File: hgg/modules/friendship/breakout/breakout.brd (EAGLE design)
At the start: 91 x 29.5 mm, 7 parts, among them IC1 MAX481CSA, IC2 MAX481CSA

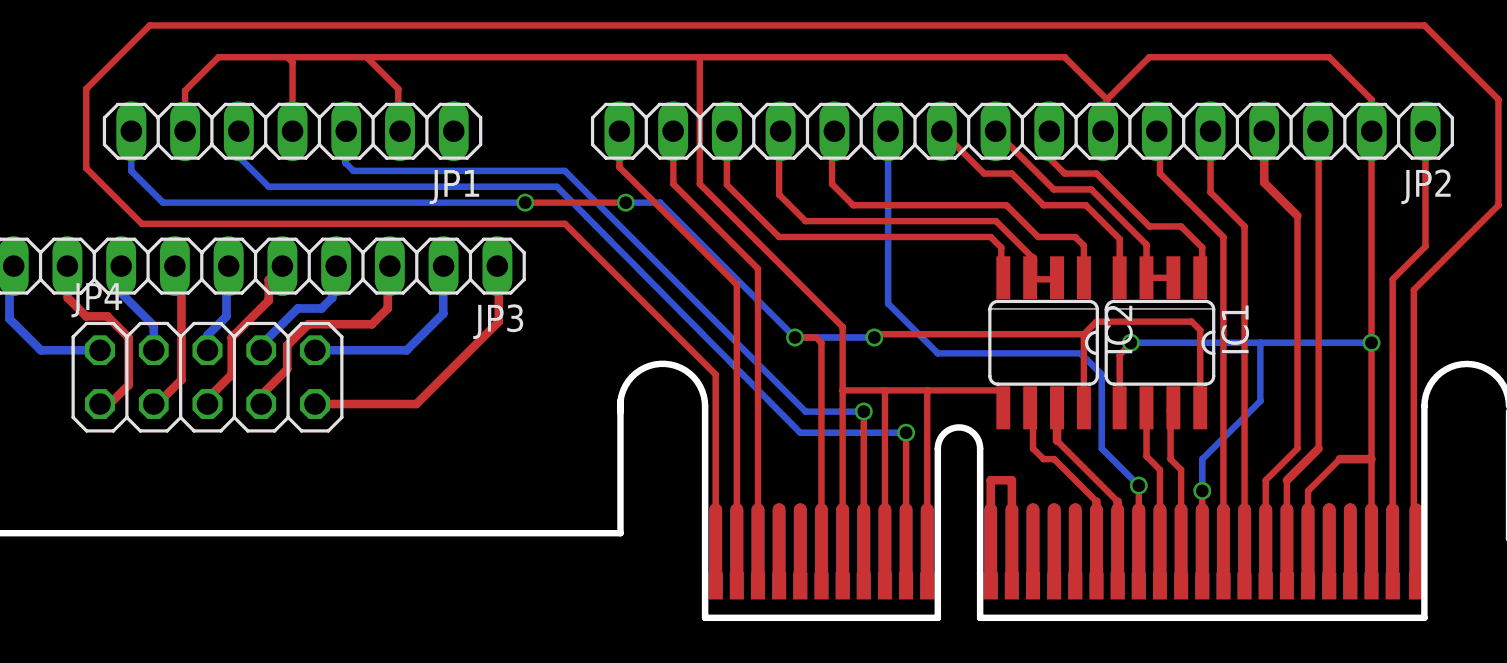
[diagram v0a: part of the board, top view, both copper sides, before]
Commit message: max485 now running @ 5V vcc
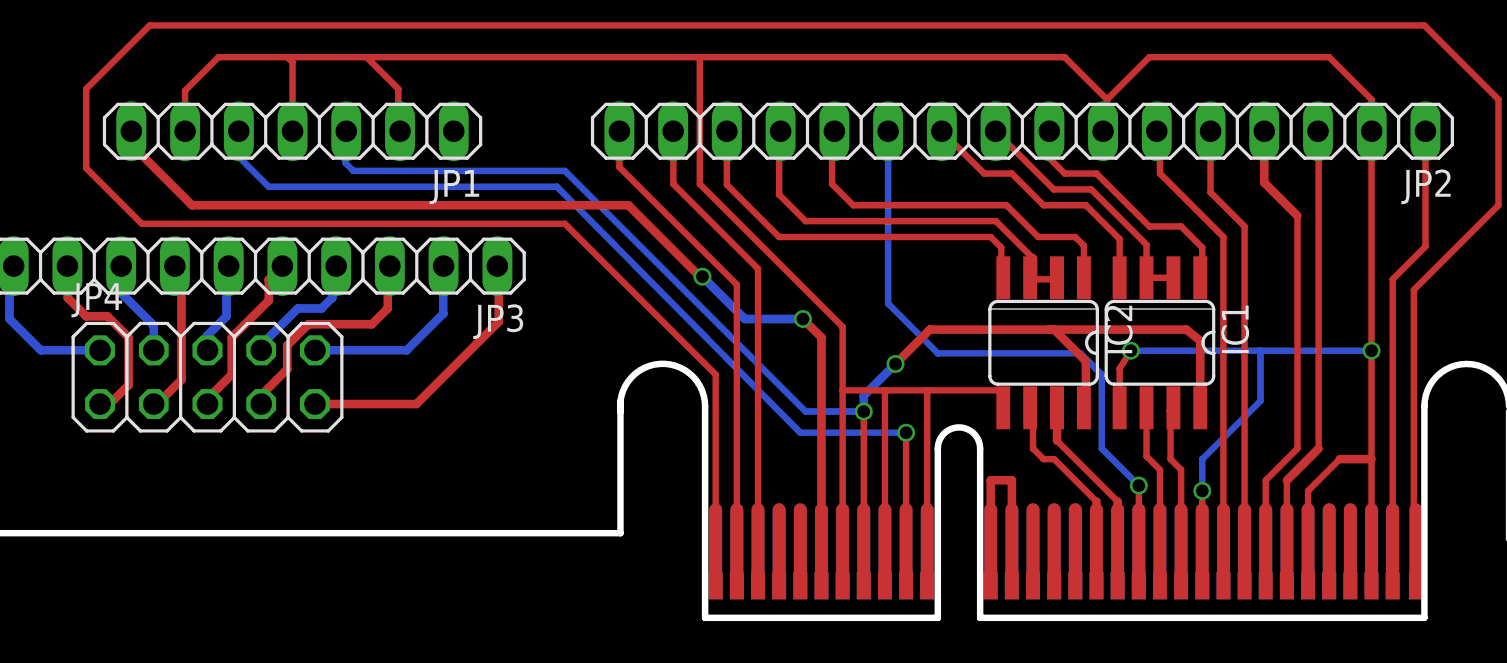
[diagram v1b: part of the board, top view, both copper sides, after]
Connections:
- removed net N$18: JP1.3, U$1.A08(+5V)
- new net 3V3: JP1.7, U$1.A06(+3V3)
- net VCC: now also JP1.3, U$1.A08(+5V); no longer JP1.7, U$1.A06(+3V3)
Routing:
- net 3V3: track 0.00 -> 48.8 mm, vias 0 -> 2
- net N$18: track 39.1 -> 0.00 mm, vias 1 -> 0
- net VCC: track 76.1 -> 64.8 mm, vias 4 -> 2
- net GND: track 183.7 -> 182.9 mm
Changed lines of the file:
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@@
 <wire x1="76.5" y1="24.5" x2="76.5" y2="23.01" width="0.3048" layer="1"/>
 <wire x1="76.5" y1="23.01" x2="76.51" y2="23" width="0.4064" layer="1"/>
-<via x="76.5" y="13" extent="1-16" drill="0.6"/>
-<wire x1="65.125" y1="13" x2="71.25" y2="13" width="0.3048" layer="16"/>
-<wire x1="71.25" y1="13" x2="76.5" y2="13" width="0.3048" layer="16"/>
-<wire x1="76.5" y1="13" x2="76.5" y2="22.99" width="0.3048" layer="1"/>
+<via x="76.5" y="12.625" extent="1-16" drill="0.6"/>
+<wire x1="65.125" y1="12.625" x2="71.25" y2="12.625" width="0.3048" layer="16"/>
+<wire x1="71.25" y1="12.625" x2="76.5" y2="12.625" width="0.3048" layer="16"/>
+<wire x1="76.5" y1="12.625" x2="76.5" y2="22.99" width="0.3048" layer="1"/>
 <wire x1="76.5" y1="22.99" x2="76.51" y2="23" width="0.4064" layer="1"/>
 <wire x1="76.5" y1="1.51" x2="76.5" y2="7.5" width="0.3048" layer="1"/>
-<wire x1="76.5" y1="7.5" x2="76.5" y2="13" width="0.3048" layer="1"/>
+<wire x1="76.5" y1="7.5" x2="76.5" y2="12.625" width="0.3048" layer="1"/>
 <wire x1="73.5" y1="1.51" x2="73.5" y2="6" width="0.3048" layer="1"/>
 <wire x1="73.5" y1="6" x2="75" y2="7.5" width="0.3048" layer="1"/>
@@
 <wire x1="68.5" y1="6" x2="68.5" y2="7.5" width="0.3048" layer="16"/>
 <wire x1="68.5" y1="7.5" x2="71.25" y2="10.25" width="0.3048" layer="16"/>
-<wire x1="71.25" y1="10.25" x2="71.25" y2="13" width="0.3048" layer="16"/>
-<wire x1="64.595" y1="9.9266" x2="64.595" y2="12.405" width="0.3048" layer="1"/>
-<wire x1="64.595" y1="12.405" x2="65.125" y2="13" width="0.3048" layer="1"/>
-<via x="65.125" y="13" extent="1-16" drill="0.6"/>
+<wire x1="71.25" y1="10.25" x2="71.25" y2="12.625" width="0.3048" layer="16"/>
+<wire x1="64.595" y1="9.9266" x2="64.595" y2="11.78" width="0.3048" layer="1"/>
+<wire x1="64.595" y1="11.78" x2="65.125" y2="12.625" width="0.3048" layer="1"/>
+<via x="65.125" y="12.625" extent="1-16" drill="0.6"/>
 <wire x1="51.5" y1="1.51" x2="51.5" y2="10.75" width="0.3048" layer="1"/>
 <contactref element="U$1" pad="A09(GND)"/>
@@
 <contactref element="IC1" pad="8"/>
 <contactref element="IC2" pad="8"/>
-<wire x1="62.905" y1="9.9266" x2="62.905" y2="13.405" width="0.3048" layer="1"/>
-<wire x1="62.905" y1="13.405" x2="63.5" y2="14" width="0.3048" layer="1"/>
-<wire x1="68.405" y1="9.9266" x2="68.405" y2="13.595" width="0.3048" layer="1"/>
-<wire x1="68.405" y1="13.595" x2="68" y2="14" width="0.3048" layer="1"/>
-<wire x1="63.5" y1="14" x2="68" y2="14" width="0.3048" layer="1"/>
-<contactref element="U$1" pad="A06(+3V3)"/>
-<wire x1="50.5" y1="1.51" x2="50.5" y2="13" width="0.3048" layer="1"/>
-<contactref element="JP1" pad="7"/>
-<wire x1="17.88" y1="23" x2="17.88" y2="21.12" width="0.3048" layer="16"/>
-<wire x1="17.88" y1="21.12" x2="19.375" y2="19.625" width="0.3048" layer="16"/>
-<wire x1="19.375" y1="19.625" x2="36.5" y2="19.625" width="0.3048" layer="16"/>
-<via x="36.5" y="19.625" extent="1-16" drill="0.6"/>
-<wire x1="36.5" y1="19.625" x2="41.25" y2="19.625" width="0.3048" layer="1"/>
-<via x="41.25" y="19.625" extent="1-16" drill="0.6"/>
-<wire x1="41.25" y1="19.625" x2="42.875" y2="19.625" width="0.3048" layer="16"/>
-<wire x1="42.875" y1="19.625" x2="49.25" y2="13.25" width="0.3048" layer="16"/>
-<via x="49.25" y="13.25" extent="1-16" drill="0.6"/>
-<wire x1="49.25" y1="13.25" x2="50.25" y2="13.25" width="0.3048" layer="1"/>
-<wire x1="50.25" y1="13.25" x2="50.5" y2="13" width="0.3048" layer="1"/>
-<wire x1="62.905" y1="13.405" x2="53.155" y2="13.405" width="0.3048" layer="1"/>
-<wire x1="53.155" y1="13.405" x2="53" y2="13.25" width="0.3048" layer="1"/>
-<via x="53" y="13.25" extent="1-16" drill="0.6"/>
-<wire x1="53" y1="13.25" x2="49.25" y2="13.25" width="0.3048" layer="16"/>
+<contactref element="U$1" pad="A08(+5V)"/>
+<contactref element="JP1" pad="3"/>
+<wire x1="52.5" y1="1.51" x2="52.5" y2="9.75" width="0.3048" layer="1"/>
+<via x="52.5" y="9.75" extent="1-16" drill="0.6"/>
+<wire x1="52.5" y1="9.75" x2="49.75" y2="9.75" width="0.3048" layer="16"/>
+<wire x1="49.75" y1="9.75" x2="38.375" y2="21.125" width="0.3048" layer="16"/>
+<wire x1="38.375" y1="21.125" x2="28.375" y2="21.125" width="0.3048" layer="16"/>
+<wire x1="28.375" y1="21.125" x2="28" y2="21.5" width="0.3048" layer="16"/>
+<wire x1="28" y1="21.5" x2="28" y2="22.71" width="0.3048" layer="16"/>
+<wire x1="28" y1="22.71" x2="28.04" y2="23" width="0.3048" layer="16"/>
+<wire x1="52.5" y1="9.75" x2="52.5" y2="10.5" width="0.4064" layer="16"/>
+<wire x1="52.5" y1="10.5" x2="54" y2="12" width="0.4064" layer="16"/>
+<via x="54" y="12" extent="1-16" drill="0.6"/>
+<wire x1="54" y1="12" x2="55.625" y2="13.625" width="0.4064" layer="1"/>
+<wire x1="55.625" y1="13.625" x2="61.25" y2="13.625" width="0.4064" layer="1"/>
+<wire x1="61.375" y1="13.625" x2="61.5" y2="13.625" width="0.4064" layer="1"/>
+<wire x1="61.5" y1="13.625" x2="63" y2="12.125" width="0.4064" layer="1"/>
+<wire x1="63" y1="12.125" x2="63" y2="10.0216" width="0.4064" layer="1"/>
+<wire x1="63" y1="10.0216" x2="62.905" y2="9.9266" width="0.4064" layer="1"/>
+<wire x1="68.405" y1="9.9266" x2="68.405" y2="13.095" width="0.4064" layer="1"/>
+<wire x1="68.405" y1="13.095" x2="67.75" y2="13.625" width="0.4064" layer="1"/>
+<wire x1="67.75" y1="13.625" x2="61.5" y2="13.625" width="0.4064" layer="1"/>
+<wire x1="61.375" y1="13.625" x2="61.25" y2="13.625" width="0.4064" layer="1"/>
 </signal>
 <signal name="N$15">
@@
 <wire x1="54.5" y1="8.75" x2="54.5" y2="1.51" width="0.3048" layer="1"/>
 </signal>
-<signal name="N$18">
-<contactref element="U$1" pad="A08(+5V)"/>
-<contactref element="JP1" pad="3"/>
-<wire x1="52.5" y1="1.51" x2="52.5" y2="9.75" width="0.3048" layer="1"/>
-<via x="52.5" y="9.75" extent="1-16" drill="0.6"/>
-<wire x1="52.5" y1="9.75" x2="49.75" y2="9.75" width="0.3048" layer="16"/>
-<wire x1="49.75" y1="9.75" x2="38.375" y2="21.125" width="0.3048" layer="16"/>
-<wire x1="38.375" y1="21.125" x2="28.375" y2="21.125" width="0.3048" layer="16"/>
-<wire x1="28.375" y1="21.125" x2="28" y2="21.5" width="0.3048" layer="16"/>
-<wire x1="28" y1="21.5" x2="28" y2="22.71" width="0.3048" layer="16"/>
-<wire x1="28" y1="22.71" x2="28.04" y2="23" width="0.3048" layer="16"/>
-</signal>
 <signal name="N$22">
 <contactref element="JP4" pad="2"/>
@@
 <wire x1="35.25" y1="16.555" x2="35.18" y2="16.625" width="0.4064" layer="1"/>
 </signal>
+<signal name="3V3">
+<contactref element="U$1" pad="A06(+3V3)"/>
+<contactref element="JP1" pad="7"/>
+<wire x1="50.5" y1="1.51" x2="50.5" y2="13.25" width="0.4064" layer="1"/>
+<wire x1="50.5" y1="13.25" x2="49.625" y2="14.125" width="0.4064" layer="1"/>
+<via x="49.625" y="14.125" extent="1-16" drill="0.6"/>
+<wire x1="49.625" y1="14.125" x2="46.875" y2="14.125" width="0.4064" layer="16"/>
+<wire x1="46.875" y1="14.125" x2="44.875" y2="16.125" width="0.4064" layer="16"/>
+<via x="44.875" y="16.125" extent="1-16" drill="0.6"/>
+<wire x1="44.875" y1="16.125" x2="44.75" y2="16.125" width="0.4064" layer="1"/>
+<wire x1="44.75" y1="16.125" x2="41.375" y2="19.5" width="0.4064" layer="1"/>
+<wire x1="41.375" y1="19.5" x2="20.75" y2="19.5" width="0.4064" layer="1"/>
+<wire x1="20.75" y1="19.5" x2="17.875" y2="22.375" width="0.4064" layer="1"/>
+<wire x1="17.875" y1="22.375" x2="17.875" y2="22.995" width="0.4064" layer="1"/>
+<wire x1="17.875" y1="22.995" x2="17.88" y2="23" width="0.4064" layer="1"/>
+</signal>
 </signals>

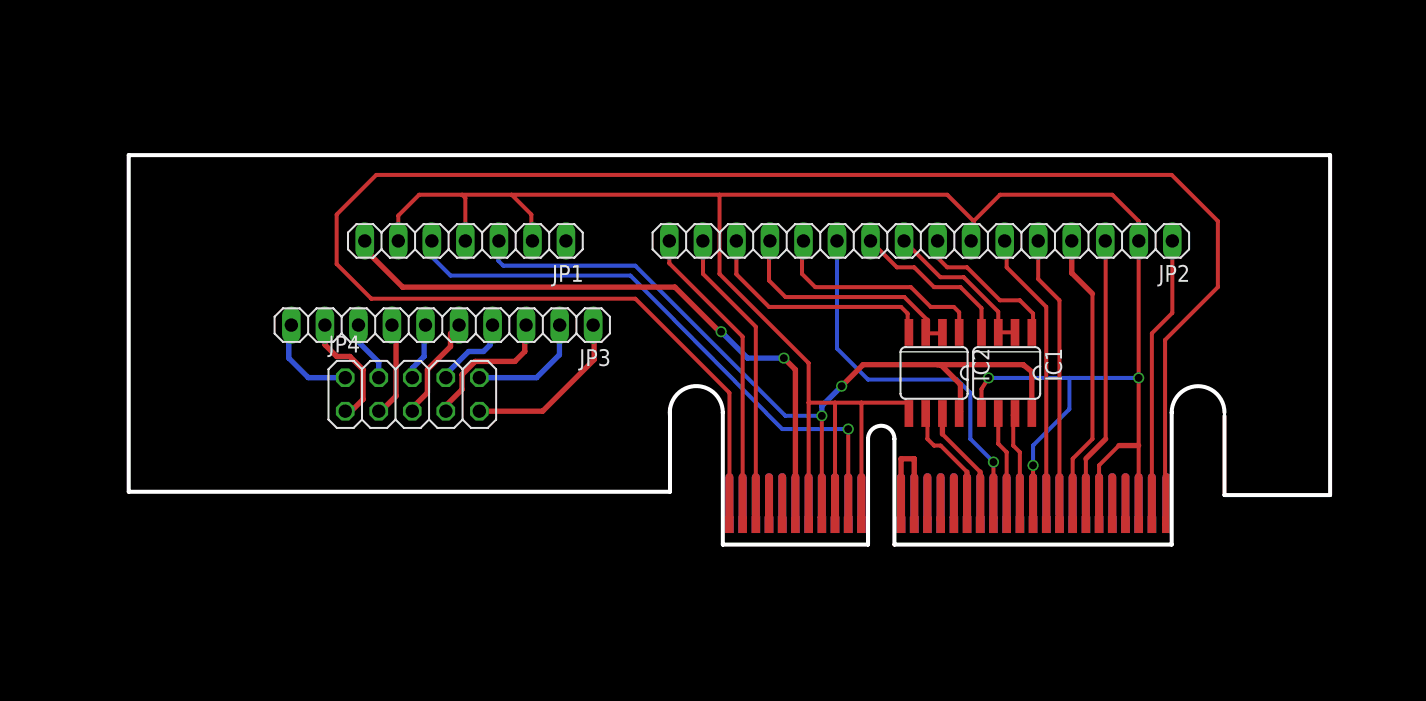
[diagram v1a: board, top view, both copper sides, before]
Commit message: swapped sides of the pcb
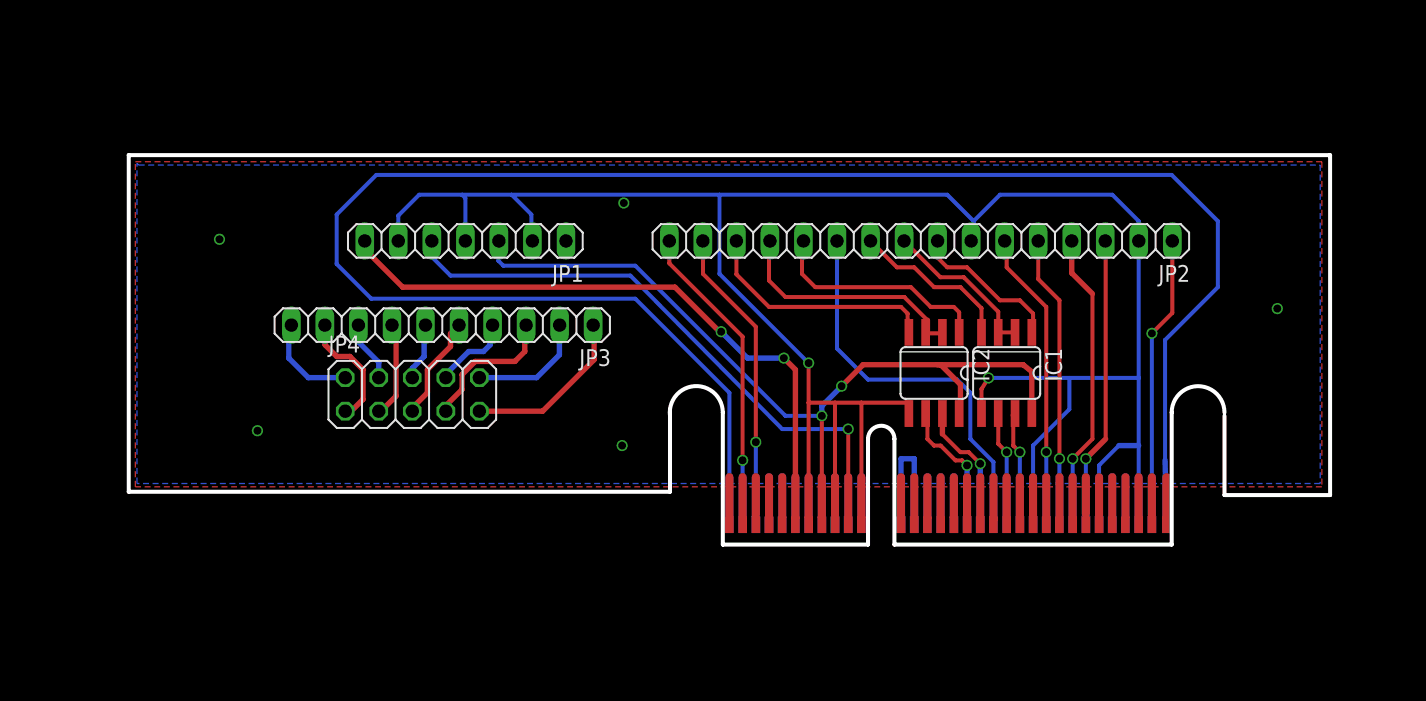
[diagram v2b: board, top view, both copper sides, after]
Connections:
- removed net N$13: JP1.5, U$1.A10(+12V)
- new net 12V: JP1.5, U$1.B10(+12V)
- net 3V3: now also U$1.B06(+3V3); no longer U$1.A06(+3V3)
- net GND: now also U$1.B07(GND), U$1.B09(GND), U$1.B11(GND); no longer U$1.A07(GND), U$1.A09(GND), U$1.A11(GND)
- net VCC: no longer U$1.A08(+5V)
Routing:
- net N$13: track 45.4 -> 0.00 mm, vias 1 -> 0
- net 12V: track 0.00 -> 45.4 mm, vias 0 -> 1
- net GND: track 182.9 -> 182.4 mm, vias 3 -> 9
- net N$3: track 9.60 -> 9.97 mm, vias 0 -> 1
- net N$2: track 10.0 -> 10.3 mm, vias 0 -> 1
- net N$19: vias 0 -> 1
- net N$9: vias 0 -> 1
- net N$7: vias 0 -> 1
- net N$6: vias 0 -> 1
- net N$5: vias 0 -> 1
- net N$23: vias 0 -> 1
- net N$21: vias 0 -> 1
- net N$20: vias 0 -> 1
- net N$17: vias 0 -> 1
- net N$10: vias 1 -> 0
- added copper zone on layer 1, net GND
- added copper zone on layer 16, net GND

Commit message: few improvements
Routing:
- net N$23: vias 1 -> 0
- net N$20: vias 1 -> 2
- net N$19: vias 1 -> 2
- net N$17: vias 1 -> 2
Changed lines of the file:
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@@
 <contactref element="IC2" pad="6"/>
 <wire x1="63.5" y1="1.51" x2="63.5" y2="6" width="0.4064" layer="16"/>
-<wire x1="63.5" y1="6" x2="63.125" y2="6.375" width="0.3048" layer="1"/>
-<wire x1="63.125" y1="6.375" x2="62.625" y2="6.375" width="0.3048" layer="1"/>
-<wire x1="62.625" y1="6.375" x2="61.5" y2="7.5" width="0.3048" layer="1"/>
-<wire x1="61.5" y1="7.5" x2="61" y2="7.5" width="0.3048" layer="1"/>
-<wire x1="61" y1="7.5" x2="60.5" y2="8" width="0.3048" layer="1"/>
+<wire x1="63.5" y1="6" x2="63.125" y2="6.375" width="0.3048" layer="16"/>
+<wire x1="63.125" y1="6.375" x2="62.25" y2="6.375" width="0.3048" layer="16"/>
+<wire x1="62.25" y1="6.375" x2="61.125" y2="7.5" width="0.3048" layer="16"/>
+<wire x1="61.125" y1="7.5" x2="60.5" y2="8" width="0.3048" layer="1"/>
 <wire x1="60.5" y1="8" x2="60.5" y2="10" width="0.3048" layer="1"/>
-<via x="63.5" y="6" extent="1-16" drill="0.6"/>
 <wire x1="60.5" y1="10" x2="60.365" y2="9.9266" width="0" layer="19" extent="1-1"/>
+<via x="61.125" y="7.5" extent="1-16" drill="0.6"/>
 </signal>
 <signal name="N$3">
@@
 <wire x1="69.5" y1="1.51" x2="69.5" y2="7.01" width="0.3048" layer="16"/>
 <wire x1="69.5" y1="7.01" x2="69.5" y2="18" width="0.3048" layer="1"/>
-<wire x1="69.5" y1="18" x2="66.5" y2="21" width="0.3048" layer="1"/>
-<wire x1="66.5" y1="21" x2="66.5" y2="22.85" width="0.3048" layer="1"/>
-<wire x1="66.5" y1="22.85" x2="66.35" y2="23" width="0.4064" layer="1"/>
+<wire x1="69.5" y1="18" x2="66.5" y2="21" width="0.3048" layer="16"/>
+<wire x1="66.5" y1="21" x2="66.5" y2="22.85" width="0.3048" layer="16"/>
+<wire x1="66.5" y1="22.85" x2="66.35" y2="23" width="0.4064" layer="16"/>
 <via x="69.5" y="7.01" extent="1-16" drill="0.6"/>
+<via x="69.5" y="18" extent="1-16" drill="0.6"/>
 </signal>
 <signal name="N$19">
 <contactref element="U$1" pad="A24(SLOWCLKCLK)"/>
 <contactref element="JP2" pad="5"/>
-<wire x1="68.89" y1="23" x2="68.89" y2="20.11" width="0.3048" layer="1"/>
-<wire x1="68.89" y1="20.11" x2="70.5" y2="18.5" width="0.3048" layer="1"/>
+<wire x1="68.89" y1="23" x2="68.89" y2="20.11" width="0.3048" layer="16"/>
+<wire x1="68.89" y1="20.11" x2="70.5" y2="18.5" width="0.3048" layer="16"/>
 <wire x1="70.5" y1="18.5" x2="70.5" y2="6.51" width="0.3048" layer="1"/>
 <wire x1="70.5" y1="6.51" x2="70.5" y2="1.51" width="0.3048" layer="16"/>
 <via x="70.5" y="6.51" extent="1-16" drill="0.6"/>
+<via x="70.5" y="18.5" extent="1-16" drill="0.6"/>
 </signal>
 <signal name="N$20">
 <contactref element="U$1" pad="A25(SLOWCLK/CS)"/>
 <contactref element="JP2" pad="4"/>
-<wire x1="71.43" y1="23" x2="71.43" y2="20.57" width="0.4064" layer="1"/>
-<wire x1="71.43" y1="20.57" x2="73" y2="19" width="0.4064" layer="1"/>
+<wire x1="71.43" y1="23" x2="71.43" y2="20.57" width="0.4064" layer="16"/>
+<wire x1="71.43" y1="20.57" x2="73" y2="19" width="0.4064" layer="16"/>
 <wire x1="73" y1="19" x2="73" y2="8" width="0.3048" layer="1"/>
 <wire x1="73" y1="8" x2="71.5" y2="6.5" width="0.3048" layer="1"/>
 <wire x1="71.5" y1="6.5" x2="71.5" y2="1.51" width="0.3048" layer="16"/>
 <via x="71.5" y="6.5" extent="1-16" drill="0.6"/>
+<via x="73" y="19" extent="1-16" drill="0.6"/>
 </signal>
 <signal name="N$21">
@@
 <contactref element="U$1" pad="A31(FASTCLK3V3)"/>
 <contactref element="JP2" pad="1"/>
-<wire x1="79.05" y1="23" x2="79.05" y2="17.55" width="0.3048" layer="1"/>
-<wire x1="79.05" y1="17.55" x2="77.5" y2="16" width="0.3048" layer="1"/>
+<wire x1="79.05" y1="23" x2="79.05" y2="17.55" width="0.3048" layer="16"/>
+<wire x1="79.05" y1="17.55" x2="77.5" y2="16" width="0.3048" layer="16"/>
 <wire x1="77.5" y1="16" x2="77.5" y2="1.51" width="0.3048" layer="16"/>
-<via x="77.5" y="16" extent="1-16" drill="0.6"/>
 </signal>
 <signal name="VCC">
